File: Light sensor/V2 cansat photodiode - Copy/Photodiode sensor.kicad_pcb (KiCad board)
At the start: 4 copper layers, 29.3 x 27.5 mm, 22 parts, among them IC1 MCP6004-I_SL, J1 Conn_01x02, J2 Conn_01x05, J3 Conn_01x04

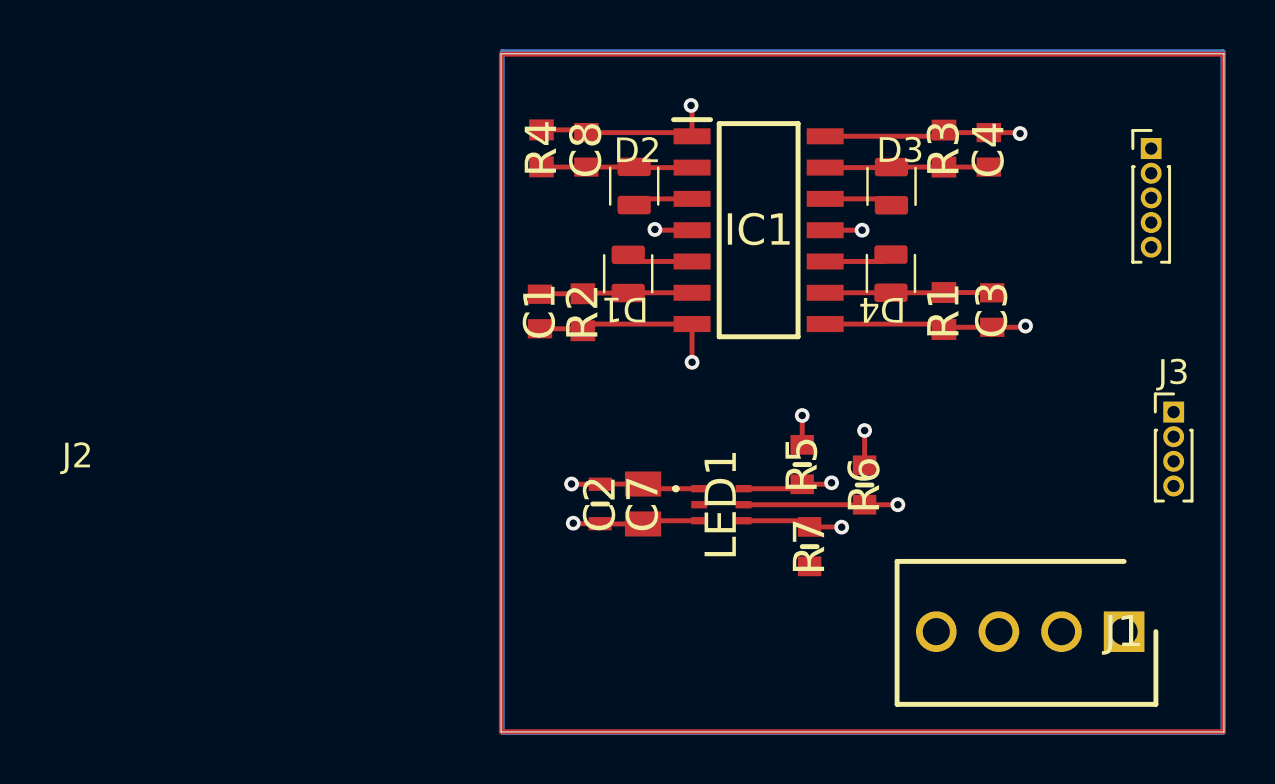
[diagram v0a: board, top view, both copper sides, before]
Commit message: V4 photodiode sensor
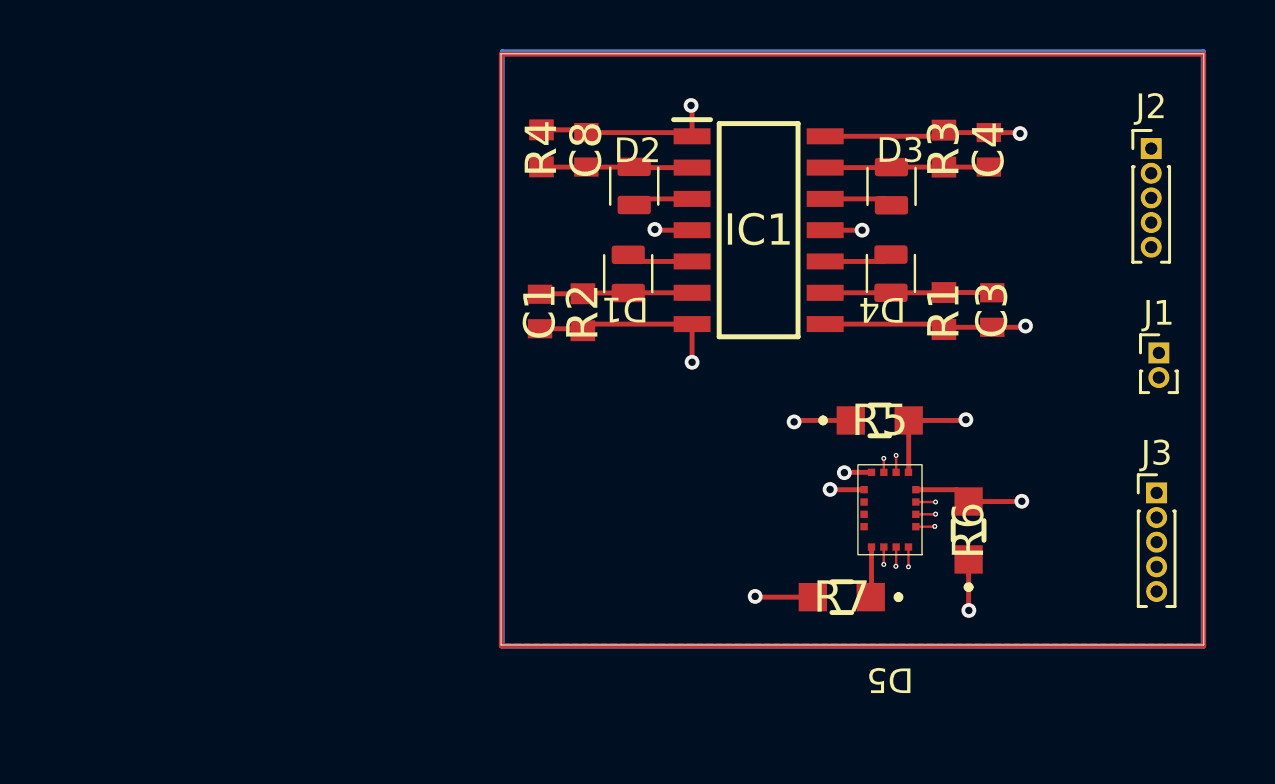
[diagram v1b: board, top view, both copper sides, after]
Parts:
- removed C2: C1608X5R1E475K080AC, CUSTOM_LIBRARY:CAPC1608X80N
- removed C7: KAM21BR71H104JM, CUSTOM_LIBRARY:CAPC2012X94N
- removed LED1: LTR-390UV-01, CUSTOM_LIBRARY:LTR390UV01
- added D5: ~, CUSTOM_LIBRARY:AS7331-AQFM, F.Cu at (156.2, 125.7)
- J1: footprint CUSTOM_LIBRARY:SHDR4W64P0X254_1X4_1020X580X1175P -> Connector_PinHeader_1.00mm:PinHeader_1x02_P1.00mm_Vertical
- J3: value Conn_01x04 -> Conn_01x05; footprint Connector_PinHeader_1.00mm:PinHeader_1x04_P1.00mm_Vertical -> Connector_PinHeader_1.00mm:PinHeader_1x05_P1.00mm_Vertical
- R5, R6: value RC0603JR-0710KL -> ERJHP6J821V; footprint CUSTOM_LIBRARY:RESC1608X55N -> CUSTOM_LIBRARY:ERJHP6D1000V
- R7: value RC0603JR-0710KL -> RC0402JR-073M3L; footprint CUSTOM_LIBRARY:RESC1608X55N -> CUSTOM_LIBRARY:ERJHP6D1000V
- moved J1 11.4 mm to (167.1, 112.9), turned to 0 degrees
- moved R6 4.61 mm to (159.4, 120.1)
- moved R5 3.62 mm to (155.8, 115.7), turned to 0 degrees
- moved J3 3.35 mm to (167.0, 118.6)
- moved R7 2.43 mm to (154.2, 122.8), turned to 180 degrees
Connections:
- J3 pad 1: Net-(J3-Pin_1) -> /READY
- J3 pad 2: GND -> /SDA
- J3 pad 3: Net-(J3-Pin_3) -> GND
- J3 pad 4: Net-(J3-Pin_4) -> /SCL
- R5 pad 1: Net-(J3-Pin_1) -> /3.3V
- R5 pad 2: /3.3V -> /SDA
- R6 pad 1: Net-(J3-Pin_3) -> /3.3V
- R6 pad 2: /3.3V -> /SCL
- R7 pad 1: Net-(J3-Pin_4) -> Net-(D5-REXT)
- R7 pad 2: /3.3V -> GND
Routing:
- net Net-(J3-Pin_1): track 18.7 -> 0.00 mm, vias 1 -> 0
- net Net-(J3-Pin_4): track 18.2 -> 0.00 mm, vias 1 -> 0
- net Net-(J3-Pin_3): track 18.2 -> 0.00 mm, vias 1 -> 0
- net /READY: track 0.00 -> 16.4 mm, vias 0 -> 1
- net /SYN: track 0.00 -> 16.3 mm, vias 0 -> 1
- net /SDA: track 0.00 -> 13.9 mm, vias 0 -> 1
- net /SCL: track 0.00 -> 11.1 mm, vias 0 -> 1
- net /3.3V: track 9.37 -> 7.17 mm, vias 4 -> 5
- net Net-(D5-REXT): track 0.00 -> 2.05 mm
- net GND: track 17.4 -> 19.3 mm, vias 2 -> 8
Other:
- board size 29.3 x 27.5 mm -> 28.5 x 24 mm
